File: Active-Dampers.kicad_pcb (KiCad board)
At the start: 2 copper layers, 16 parts, among them IC6 MCP25625-E_ML, J9 M50-3630242R, U1 ESP32-S3-WROOM-1, U2 DRV8848, U3 DRV8848, U4 L80-R, Y3 X50328MSB2GI

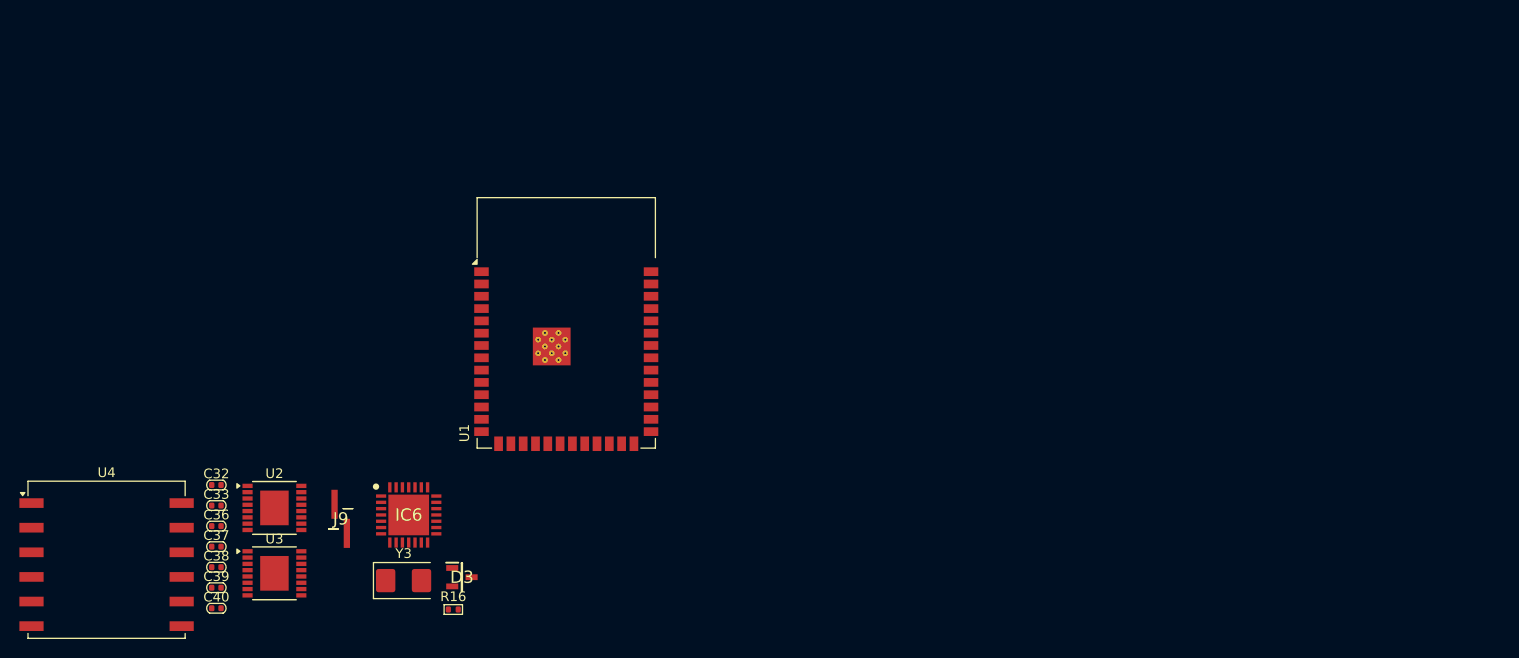
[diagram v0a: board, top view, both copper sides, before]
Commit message: redo design to esp32
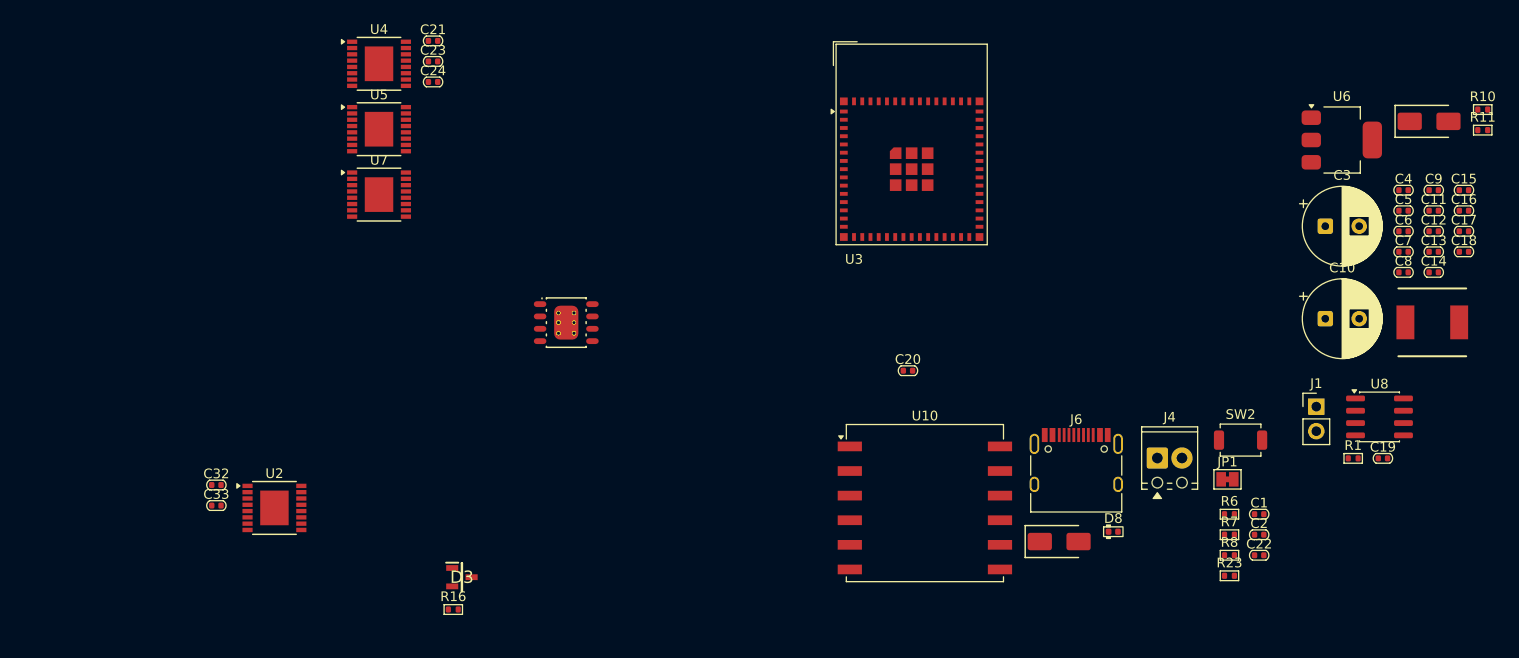
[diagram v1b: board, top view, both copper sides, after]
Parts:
- removed C36, C37: 22pF, PCM_Capacitor_SMD_AKL:C_0402_1005Metric
- removed C38, C39, C40: 0.1uF, PCM_Capacitor_SMD_AKL:C_0402_1005Metric
- removed IC6: MCP25625-E_ML, SamacSys_Parts:QFN65P600X600X100-29N-D
- removed J9: M50-3630242R, SamacSys_Parts:M503630242R
- removed Y3: X50328MSB2GI, Crystal:Crystal_SMD_5032-2Pin_5.0x3.2mm
- added C1: 1uF, PCM_Capacitor_SMD_AKL:C_0402_1005Metric, F.Cu at (222.4, 89.2)
- added C10: 220uF, Capacitor_THT:CP_Radial_D8.0mm_P3.50mm, F.Cu at (229.2, 69.0)
- added C11: 22uF, PCM_Capacitor_SMD_AKL:C_0402_1005Metric, F.Cu at (240.4, 57.8)
- added C12: 22uF, PCM_Capacitor_SMD_AKL:C_0402_1005Metric, F.Cu at (240.4, 60.0)
- added C13: 22uF, PCM_Capacitor_SMD_AKL:C_0402_1005Metric, F.Cu at (240.4, 62.1)
- added C14: 100nF, PCM_Capacitor_SMD_AKL:C_0402_1005Metric, F.Cu at (240.4, 64.2)
- added C15: 22uF, PCM_Capacitor_SMD_AKL:C_0402_1005Metric, F.Cu at (243.6, 55.7)
- added C16: 22uF, PCM_Capacitor_SMD_AKL:C_0402_1005Metric, F.Cu at (243.6, 57.8)
- added C17: 22uF, PCM_Capacitor_SMD_AKL:C_0402_1005Metric, F.Cu at (243.6, 60.0)
- added C18: 22uF, PCM_Capacitor_SMD_AKL:C_0402_1005Metric, F.Cu at (243.6, 62.1)
- added C19: 0.1uF, PCM_Capacitor_SMD_AKL:C_0402_1005Metric, F.Cu at (235.2, 83.4)
- added C2: 10uF, PCM_Capacitor_SMD_AKL:C_0402_1005Metric, F.Cu at (222.4, 91.3)
- added C20: 2.2uF, PCM_Capacitor_SMD_AKL:C_0402_1005Metric, F.Cu at (186.2, 74.3)
- added C21: 2.2uF, PCM_Capacitor_SMD_AKL:C_0402_1005Metric, F.Cu at (137.2, 40.3)
- added C22: 10uF, PCM_Capacitor_SMD_AKL:C_0402_1005Metric, F.Cu at (222.4, 93.4)
- added C23: 2.2uF, PCM_Capacitor_SMD_AKL:C_0402_1005Metric, F.Cu at (137.2, 42.4)
- added C24: 2.2uF, PCM_Capacitor_SMD_AKL:C_0402_1005Metric, F.Cu at (137.2, 44.5)
- added C3: 220uF, Capacitor_THT:CP_Radial_D8.0mm_P3.50mm, F.Cu at (229.2, 59.4)
- added C4: 22nF, PCM_Capacitor_SMD_AKL:C_0402_1005Metric, F.Cu at (237.3, 55.7)
- added C5: 22nF, PCM_Capacitor_SMD_AKL:C_0402_1005Metric, F.Cu at (237.3, 57.8)
- added C6: 22nF, PCM_Capacitor_SMD_AKL:C_0402_1005Metric, F.Cu at (237.3, 60.0)
- added C7: 22nF, PCM_Capacitor_SMD_AKL:C_0402_1005Metric, F.Cu at (237.3, 62.1)
- added C8: 22nF, PCM_Capacitor_SMD_AKL:C_0402_1005Metric, F.Cu at (237.3, 64.2)
- added C9: 10nF, PCM_Capacitor_SMD_AKL:C_0402_1005Metric, F.Cu at (240.4, 55.7)
- added D2: SS54, PCM_JLCPCB:D_SMA, F.Cu at (240.0, 48.6)
- added D8: LED BLUE, PCM_LED_SMD_AKL:LED_0402_1005Metric, F.Cu at (207.4, 91.0)
- added D9: SS54, PCM_JLCPCB:D_SMA, F.Cu at (201.8, 92.0)
- added J1: PINHD_1x2_Male, Connector_PinHeader_2.54mm:PinHeader_1x02_P2.54mm_Vertical, F.Cu at (228.3, 78.1)
- added J4: Conn_01x02, TerminalBlock_Phoenix:TerminalBlock_Phoenix_MPT-0,5-2-2.54_1x02_P2.54mm_Horizontal, F.Cu at (211.9, 83.4)
- added J6: USB_C_Receptacle_USB2.0_16P, Connector_USB:USB_C_Receptacle_HRO_TYPE-C-31-M-12, F.Cu at (203.5, 85.0)
- added JP1: SolderJumper_2_Bridged, Jumper:SolderJumper-2_P1.3mm_Bridged_Pad1.0x1.5mm, F.Cu at (219.1, 85.6)
- added L1: 15uH, PCM_SparkFun-Coil:Inductor_7.3x6.6mm, F.Cu at (240.3, 69.4)
- added R1: 10k, PCM_Resistor_SMD_AKL:R_0402_1005Metric, F.Cu at (232.1, 83.4)
- added R10: 10k, PCM_Resistor_SMD_AKL:R_0402_1005Metric, F.Cu at (245.5, 47.4)
- added R11: 3.24k, PCM_Resistor_SMD_AKL:R_0402_1005Metric, F.Cu at (245.5, 49.5)
- added R23: 1k, PCM_Resistor_SMD_AKL:R_0402_1005Metric, F.Cu at (219.4, 95.5)
- added R6: 5k1, PCM_Resistor_SMD_AKL:R_0402_1005Metric, F.Cu at (219.4, 89.2)
- added R7: 5k1, PCM_Resistor_SMD_AKL:R_0402_1005Metric, F.Cu at (219.4, 91.3)
- added R8: 2k2, PCM_Resistor_SMD_AKL:R_0402_1005Metric, F.Cu at (219.4, 93.4)
- added SW2: SW_SPST, Button_Switch_SMD:SW_SPST_TS-1088-xR025, F.Cu at (220.5, 81.5)
- added U10: L80-R, RF_GPS:Quectel_L80-R, F.Cu at (187.9, 88.0)
- added U5: DRV8848, Package_SO:TSSOP-16-1EP_4.4x5mm_P0.65mm, F.Cu at (131.6, 49.4)
- added U6: AMS1117-3.3, Package_TO_SOT_SMD:SOT-223-3_TabPin2, F.Cu at (230.9, 50.5)
- added U7: DRV8848, Package_SO:TSSOP-16-1EP_4.4x5mm_P0.65mm, F.Cu at (131.6, 56.2)
- added U8: SN65HVD230, Package_SO:SOIC-8_3.9x4.9mm_P1.27mm, F.Cu at (234.8, 79.1)
- U1: value ESP32-S3-WROOM-1 -> TPS5430DDAR; footprint RF_Module:ESP32-S3-WROOM-1 -> PCM_JLCPCB:ESOP-8_L4.9-W3.9-P1.27-LS6.0-TL-EP
- U3: value DRV8848 -> ESP32-S3-MINI-1; footprint Package_SO:TSSOP-16-1EP_4.4x5mm_P0.65mm -> RF_Module:ESP32-S2-MINI-1
- U4: value L80-R -> DRV8848; footprint RF_GPS:Quectel_L80-R -> Package_SO:TSSOP-16-1EP_4.4x5mm_P0.65mm
- moved U3 79.3 mm to (186.6, 51.0)
- moved U4 58.4 mm to (131.6, 42.7)
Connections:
- net C1_H renamed /CAN/CAN_H
- net C1_L renamed /CAN/CAN_L
- U1 pad 1: Net-(U1-GND-Pad1) -> Net-(U1-BOOT)
- U1 pad 4: unconnected-(U1-IO4-Pad4) -> Net-(U1-VSENSE)
- U1 pad 6: unconnected-(U1-IO6-Pad6) -> GND
- U1 pad 7: unconnected-(U1-IO7-Pad7) -> +12V
- U1 pad 8: unconnected-(U1-IO15-Pad8) -> Net-(U1-PH)
- U1 pad 9: unconnected-(U1-IO16-Pad9) -> GND
- U2 pad 1: unconnected-(U2-~{SLEEP}-Pad1) -> /~{SLEEP}_1
- U2 pad 10: unconnected-(U2-BIN2-Pad10) -> /BIN2_1
- U2 pad 11: unconnected-(U2-VREF-Pad11) -> +3.3V
- U2 pad 12: unconnected-(U2-VM-Pad12) -> +12V
- U2 pad 13: Net-(U2-GND-Pad13) -> GND
- U2 pad 14: unconnected-(U2-VINT-Pad14) -> Net-(U2-VINT)
- U2 pad 15: unconnected-(U2-AIN2-Pad15) -> /AIN2_1
- U2 pad 16: unconnected-(U2-AIN1-Pad16) -> /AIN1_1
- U2 pad 17: Net-(U2-GND-Pad13) -> GND
- U2 pad 2: unconnected-(U2-AOUT1-Pad2) -> /AOUT_1
- U2 pad 4: unconnected-(U2-AOUT2-Pad4) -> /AOUT_1
- U2 pad 5: unconnected-(U2-BOUT2-Pad5) -> /BOUT_1
- U2 pad 7: unconnected-(U2-BOUT1-Pad7) -> /BOUT_1
- U2 pad 8: unconnected-(U2-~{FAULT}-Pad8) -> /~{FAULT}_1
- U2 pad 9: unconnected-(U2-BIN1-Pad9) -> /BIN1_1
- U3 pad 1: unconnected-(U3-~{SLEEP}-Pad1) -> Net-(U3-GND-Pad1)
- U3 pad 13: Net-(U3-GND-Pad13) -> unconnected-(U3-IO9-Pad13)
- U3 pad 17: Net-(U3-GND-Pad13) -> unconnected-(U3-IO13-Pad17)
- U3 pad 2: unconnected-(U3-AOUT1-Pad2) -> Net-(U3-GND-Pad1)
- U3 pad 3: unconnected-(U3-AISEN-Pad3) -> +3.3V
- U3 pad 4: unconnected-(U3-AOUT2-Pad4) -> /~{FAULT}_1
- U3 pad 5: unconnected-(U3-BOUT2-Pad5) -> /~{SLEEP}_1
- U3 pad 6: unconnected-(U3-BISEN-Pad6) -> /AIN1_1
- U3 pad 7: unconnected-(U3-BOUT1-Pad7) -> /AIN2_1
- U3 pad 8: unconnected-(U3-~{FAULT}-Pad8) -> /BIN1_1
- U3 pad 9: unconnected-(U3-BIN1-Pad9) -> /BIN2_1
- U4 pad 1: unconnected-(U4-RXD1-Pad1) -> /~{SLEEP}_1
- U4 pad 10: unconnected-(U4-~{RESET}-Pad10) -> /BIN2_1
- U4 pad 11: unconnected-(U4-RESERVED-Pad11) -> +3.3V
- U4 pad 12: Net-(U4-GND-Pad12) -> +12V
- U4 pad 2: unconnected-(U4-TXD1-Pad2) -> /AOUT_1
- U4 pad 3: Net-(U4-GND-Pad12) -> unconnected-(U4-AISEN-Pad3)
- U4 pad 4: unconnected-(U4-VCC-Pad4) -> /AOUT_1
- U4 pad 5: unconnected-(U4-V_BCKP-Pad5) -> /BOUT_1
- U4 pad 7: unconnected-(U4-RESERVED-Pad7) -> /BOUT_1
- U4 pad 8: unconnected-(U4-RESERVED-Pad8) -> /~{FAULT}_1
- U4 pad 9: unconnected-(U4-NC-Pad9) -> /BIN1_1

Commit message: begin layout
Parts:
- added H1: MountingHole_M3_3.2mm_Pad, MountingHole:MountingHole_2.2mm_M2_ISO14580_Pad, F.Cu at (52.0, 98.0)
- added H2: MountingHole_M3_3.2mm_Pad, MountingHole:MountingHole_2.2mm_M2_ISO14580_Pad, F.Cu at (113.0, 98.0)
- added H3: MountingHole_M3_3.2mm_Pad, MountingHole:MountingHole_2.2mm_M2_ISO14580_Pad, F.Cu at (29.5, 58.6)
- added H4: MountingHole_M3_3.2mm_Pad, MountingHole:MountingHole_2.2mm_M2_ISO14580_Pad, F.Cu at (29.5, 64.0)
- added J2: Conn_01x04, Connector_JST:JST_XH_B4B-XH-AM_1x04_P2.50mm_Vertical, F.Cu at (65.0, 97.0)
- added J3: Conn_01x04, Connector_JST:JST_XH_B4B-XH-AM_1x04_P2.50mm_Vertical, F.Cu at (79.0, 97.0)
- added J5: Conn_01x04, Connector_JST:JST_XH_B4B-XH-AM_1x04_P2.50mm_Vertical, F.Cu at (93.4, 97.0)
- added J7: Conn_01x04, Connector_JST:JST_XH_B4B-XH-AM_1x04_P2.50mm_Vertical, F.Cu at (107.4, 97.0)
- added J8: Barrel_Jack_Switch_Pin3Ring, Connector_BarrelJack:BarrelJack_Horizontal, F.Cu at (63.8, 77.6)
- C1, C11, C12, C13, C14, C15, C16, C17, C18, C19, C2, C20, C21, C22, C23, C24, C32, C33, C4, C5, C6, C7, C8, C9: footprint PCM_Capacitor_SMD_AKL:C_0402_1005Metric -> PCM_Capacitor_SMD_AKL:C_0603_1608Metric
- R1, R10, R11, R16, R23, R6, R7, R8: footprint PCM_Resistor_SMD_AKL:R_0402_1005Metric -> PCM_Resistor_SMD_AKL:R_0603_1608Metric
- moved C10 205.4 mm to (24.0, 78.0), turned to 90 degrees
- moved R10 179.3 mm to (67.6, 70.1)
- moved R11 179.3 mm to (67.6, 72.1), turned to 180 degrees
- moved C3 177.2 mm to (54.0, 86.0), turned to -90 degrees
- moved C8 171.1 mm to (67.2, 82.4), turned to 90 degrees
- moved C9 170.5 mm to (70.6, 71.1), turned to 90 degrees
- moved C4 170.2 mm to (69.2, 82.4), turned to 90 degrees
- moved C5 167.9 mm to (71.2, 82.4), turned to 90 degrees
- moved D2 166.4 mm to (76.1, 77.6)
- moved C6 165.6 mm to (73.2, 82.4), turned to 90 degrees
- moved L1 164.2 mm to (76.1, 71.6)
- moved C7 163.3 mm to (75.2, 82.4), turned to 90 degrees
- moved U10 100.3 mm to (105.0, 31.5)
- moved U1 82.1 mm to (69.1, 76.8), turned to -90 degrees
- moved U3 80.4 mm to (109.8, 75.0), turned to -90 degrees
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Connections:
- U10 pad 1: /CAN_RX -> /GPS_RX
- U10 pad 2: /CAN_TX -> /GPS_TX
- U2 pad 2: /AOUT_1 -> /AOUT_1_1
- U2 pad 4: /AOUT_1 -> /AOUT_1_2
- U2 pad 5: /BOUT_1 -> /BOUT_1_2
- U2 pad 7: /BOUT_1 -> /BOUT_1_1
- U3 pad 1: Net-(U3-GND-Pad1) -> GND
- U3 pad 10: unconnected-(U3-IO6-Pad10) -> /~{FAULT}_2
- U3 pad 11: unconnected-(U3-IO7-Pad11) -> /~{SLEEP}_2
- U3 pad 12: unconnected-(U3-IO8-Pad12) -> /AIN1_2
- U3 pad 13: unconnected-(U3-IO9-Pad13) -> /AIN2_2
- U3 pad 14: unconnected-(U3-IO10-Pad14) -> /BIN1_2
- U3 pad 15: unconnected-(U3-IO11-Pad15) -> /BIN2_2
- U3 pad 16: unconnected-(U3-IO12-Pad16) -> /~{FAULT}_3
- U3 pad 17: unconnected-(U3-IO13-Pad17) -> /~{SLEEP}_3
- U3 pad 18: unconnected-(U3-IO14-Pad18) -> /AIN1_3
- U3 pad 19: unconnected-(U3-IO15-Pad19) -> /AIN2_3
- U3 pad 2: Net-(U3-GND-Pad1) -> GND
- U3 pad 20: unconnected-(U3-IO16-Pad20) -> /BIN1_3
- U3 pad 21: unconnected-(U3-IO17-Pad21) -> /BIN2_3
- U3 pad 25: unconnected-(U3-IO21-Pad25) -> /GPS_RX
- U3 pad 26: unconnected-(U3-IO26-Pad26) -> /GPS_TX
- U3 pad 27: unconnected-(U3-IO47-Pad27) -> /BIN1_4
- U3 pad 30: unconnected-(U3-IO48-Pad30) -> /BIN2_4
- U3 pad 37: unconnected-(U3-IO41-Pad37) -> /~{FAULT}_4
- U3 pad 38: unconnected-(U3-IO42-Pad38) -> /~{SLEEP}_4
- U3 pad 41: unconnected-(U3-IO45-Pad41) -> /AIN1_4
- U3 pad 42: Net-(U3-GND-Pad1) -> GND
- U3 pad 43: Net-(U3-GND-Pad1) -> GND
- U3 pad 44: unconnected-(U3-IO46-Pad44) -> /AIN2_4
- U3 pad 46: Net-(U3-GND-Pad1) -> GND
- U3 pad 47: Net-(U3-GND-Pad1) -> GND
- U3 pad 48: Net-(U3-GND-Pad1) -> GND
- U3 pad 49: Net-(U3-GND-Pad1) -> GND
- U3 pad 50: Net-(U3-GND-Pad1) -> GND
- U3 pad 51: Net-(U3-GND-Pad1) -> GND
- U3 pad 52: Net-(U3-GND-Pad1) -> GND
- U3 pad 53: Net-(U3-GND-Pad1) -> GND
- U3 pad 54: Net-(U3-GND-Pad1) -> GND
- U3 pad 55: Net-(U3-GND-Pad1) -> GND
- U3 pad 56: Net-(U3-GND-Pad1) -> GND
- U3 pad 57: Net-(U3-GND-Pad1) -> GND
- U3 pad 58: Net-(U3-GND-Pad1) -> GND
- U3 pad 59: Net-(U3-GND-Pad1) -> GND
- U3 pad 60: Net-(U3-GND-Pad1) -> GND
- U3 pad 61: Net-(U3-GND-Pad1) -> GND
- U3 pad 62: Net-(U3-GND-Pad1) -> GND
- U3 pad 63: Net-(U3-GND-Pad1) -> GND
- U3 pad 64: Net-(U3-GND-Pad1) -> GND
- U3 pad 65: Net-(U3-GND-Pad1) -> GND
- U4 pad 1: /~{SLEEP}_1 -> /~{SLEEP}_2
- U4 pad 10: /BIN2_1 -> /BIN2_2
- U4 pad 15: /AIN2_1 -> /AIN2_2
- U4 pad 16: /AIN1_1 -> /AIN1_2
- U4 pad 2: /AOUT_1 -> /AOUT_1_2
- U4 pad 4: /AOUT_1 -> /AOUT_2_2
- U4 pad 5: /BOUT_1 -> /BOUT_2_2
- U4 pad 7: /BOUT_1 -> /BOUT_1_2
- U4 pad 8: /~{FAULT}_1 -> /~{FAULT}_2
- U4 pad 9: /BIN1_1 -> /BIN1_2
- U5 pad 1: /~{SLEEP}_1 -> /~{SLEEP}_3
- U5 pad 10: /BIN2_1 -> /BIN2_3
- U5 pad 15: /AIN2_1 -> /AIN2_3
- U5 pad 16: /AIN1_1 -> /AIN1_3
- U5 pad 2: /AOUT_1 -> /AOUT_1_3
- U5 pad 4: /AOUT_1 -> /AOUT_2_3
- U5 pad 5: /BOUT_1 -> /BOUT_2_3
- U5 pad 7: /BOUT_1 -> /BOUT_1_3
- U5 pad 8: /~{FAULT}_1 -> /~{FAULT}_3
- U5 pad 9: /BIN1_1 -> /BIN1_3
- U7 pad 1: /~{SLEEP}_1 -> /~{SLEEP}_4
- U7 pad 10: /BIN2_1 -> /BIN2_4
- U7 pad 15: /AIN2_1 -> /AIN2_4
- U7 pad 16: /AIN1_1 -> /AIN1_4
- U7 pad 2: /AOUT_1 -> /AOUT_1_3
- U7 pad 4: /AOUT_1 -> /AOUT_2_3
- U7 pad 5: /BOUT_1 -> /BOUT_2_3
- U7 pad 7: /BOUT_1 -> /BOUT_1_3
- U7 pad 8: /~{FAULT}_1 -> /~{FAULT}_4
- U7 pad 9: /BIN1_1 -> /BIN1_4
- U8 pad 1: /TX -> /CAN_TX
- U8 pad 4: /RX -> /CAN_RX
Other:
- board outline added: 65 x 50 mm
